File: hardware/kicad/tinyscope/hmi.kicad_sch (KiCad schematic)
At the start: 51 parts, among them U10 CR2013-MI2120

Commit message: feat: hardware: Adds the user input rotary encoders description. Changes 5V pull-up to 3V3
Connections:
- net +5V is gone; now on net +3V3: R?.1, R?.1, R?.1, R?.1, R?.1, R?.1, R?.1, R?.1, R?.1, R?.1

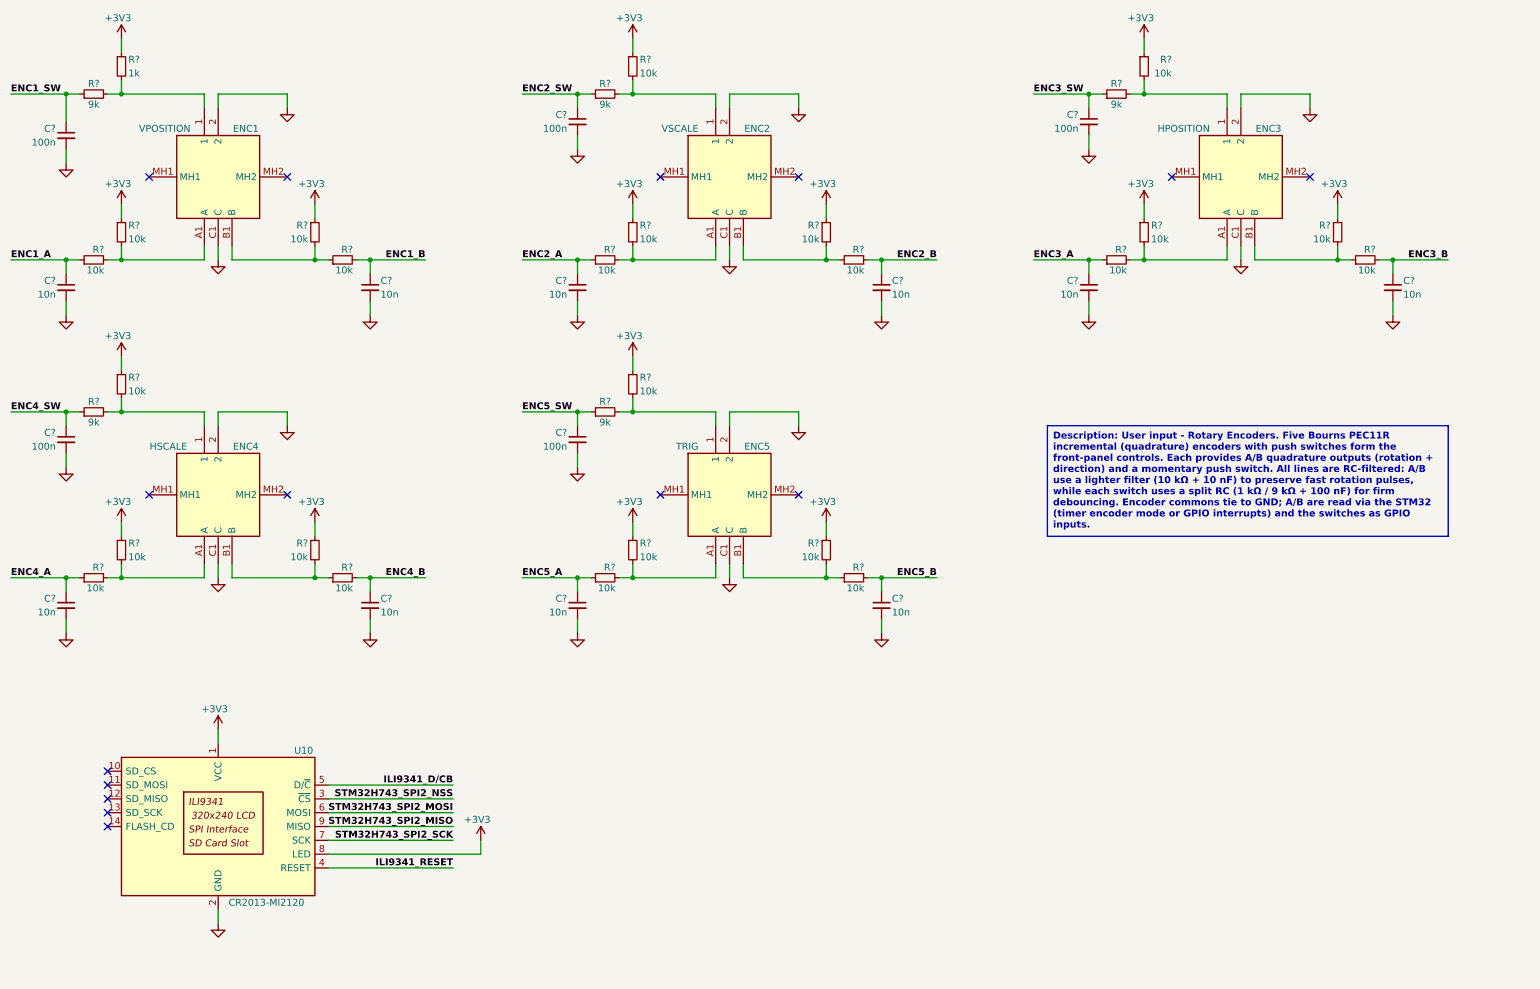
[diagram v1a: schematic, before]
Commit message: feat: hardware: Adds Waveshare 16498 display 02x17 connector. Cleans up all schematics
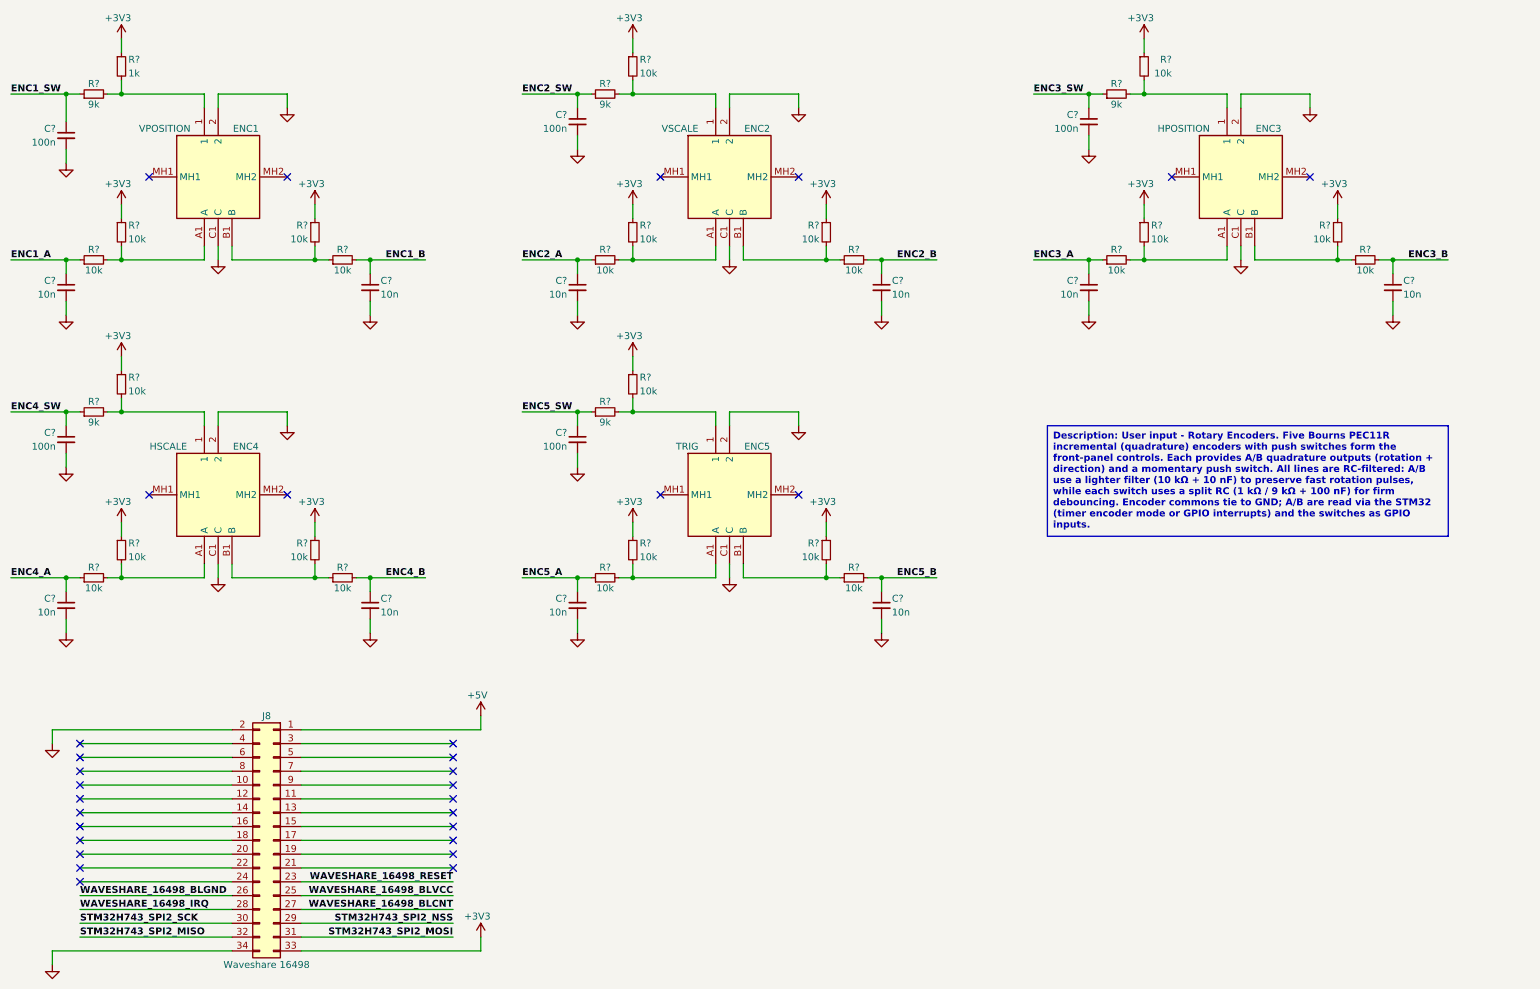
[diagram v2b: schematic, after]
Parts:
- removed U10: CR2013-MI2120, Display:CR2013-MI2120, symbol Driver_Display:CR2013-MI2120
- added J8: Waveshare 16498, symbol Connector_Generic:Conn_02x17_Odd_Even
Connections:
- net +3V3: now also J8.33 (Pin_33)
- net GND: now also J8.2 (Pin_2), J8.34 (Pin_34)
- net STM32H743_SPI2_MISO: now also J8.32 (Pin_32)
- net STM32H743_SPI2_MOSI: now also J8.31 (Pin_31)
- net STM32H743_SPI2_NSS: now also J8.29 (Pin_29)
- net STM32H743_SPI2_SCK: now also J8.30 (Pin_30)
- new net +5V: J8.1 (Pin_1)
- new net WAVESHARE_16498_BLCNT: J8.27 (Pin_27)
- new net WAVESHARE_16498_BLGND: J8.26 (Pin_26)
- new net WAVESHARE_16498_BLVCC: J8.25 (Pin_25)
- new net WAVESHARE_16498_IRQ: J8.28 (Pin_28)
- new net WAVESHARE_16498_RESET: J8.23 (Pin_23)
- no-connect marks 15 -> 31
